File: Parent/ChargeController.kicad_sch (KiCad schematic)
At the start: 1 part, among them U11 TSV911IDT

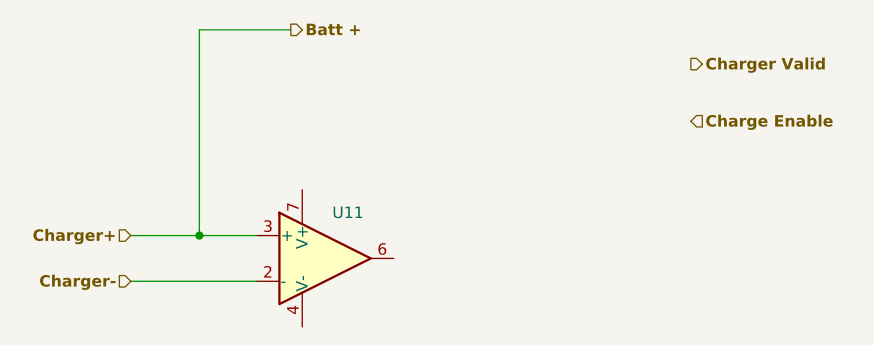
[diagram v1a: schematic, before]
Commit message: Updated Parent - Moved workspace to cloud
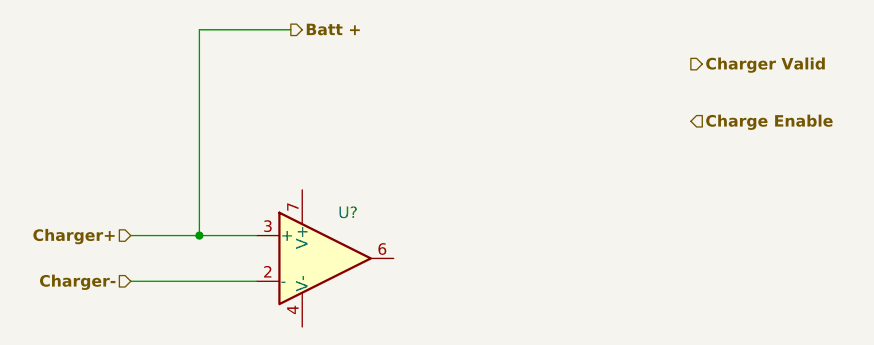
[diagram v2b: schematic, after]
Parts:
- renumbered U11 to U?
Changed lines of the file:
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@@
   (symbol (lib_id "Amplifier_Operational:TSV911IDT") (at 149.86 80.01 0) (unit 1)
     (in_bom yes) (on_board yes) (dnp no)
-    (property "Reference" "U11" (at 152.4 74.93 0)
+    (property "Reference" "U?" (at 152.4 74.93 0)
       (effects (font (size 1.27 1.27)))
     )
@@
       (project "Parent"
         (path "/1451ec1d-c665-471b-ba41-1d89ef6a63bf/19e05faa-0db5-4214-a5d0-9432a31cc835"
-          (reference "U11") (unit 1)
-        )
-        (path "/1451ec1d-c665-471b-ba41-1d89ef6a63bf/74b6a814-0062-436b-b15e-0c05f093947f"
-          (reference "U85") (unit 1)
+          (reference "U?") (unit 1)
         )
         (path "/1451ec1d-c665-471b-ba41-1d89ef6a63bf/c3abd914-8a3d-4045-89a3-4c882ae1ce0a"
-          (reference "U9") (unit 1)
+          (reference "U?") (unit 1)
         )
       )
